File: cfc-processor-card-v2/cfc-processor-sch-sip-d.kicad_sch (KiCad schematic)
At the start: 4 parts, among them J3 Conn_01x02, U7 OSD3358-1G-ISM

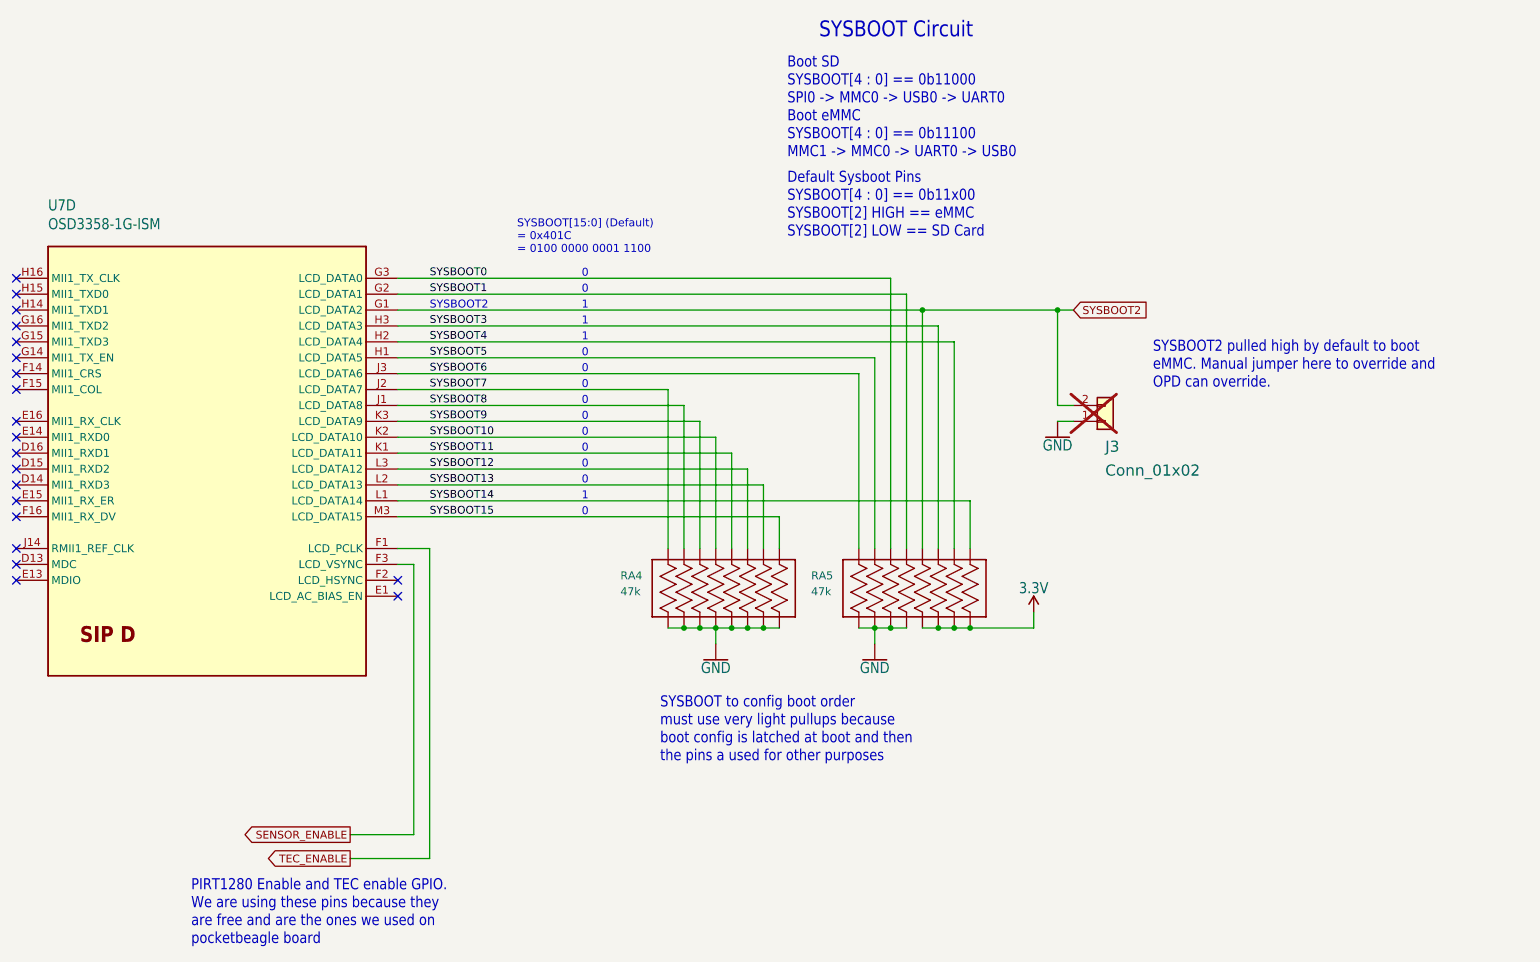
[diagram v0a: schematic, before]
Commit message: CFC processor schematic Change
changed to hierarchy view, changed all global net labels to hierarchy labels, changed all resistor, capacitor, and ground symbols to modern oresat labels. Deleted connectors sheet and added .history to gitignore.
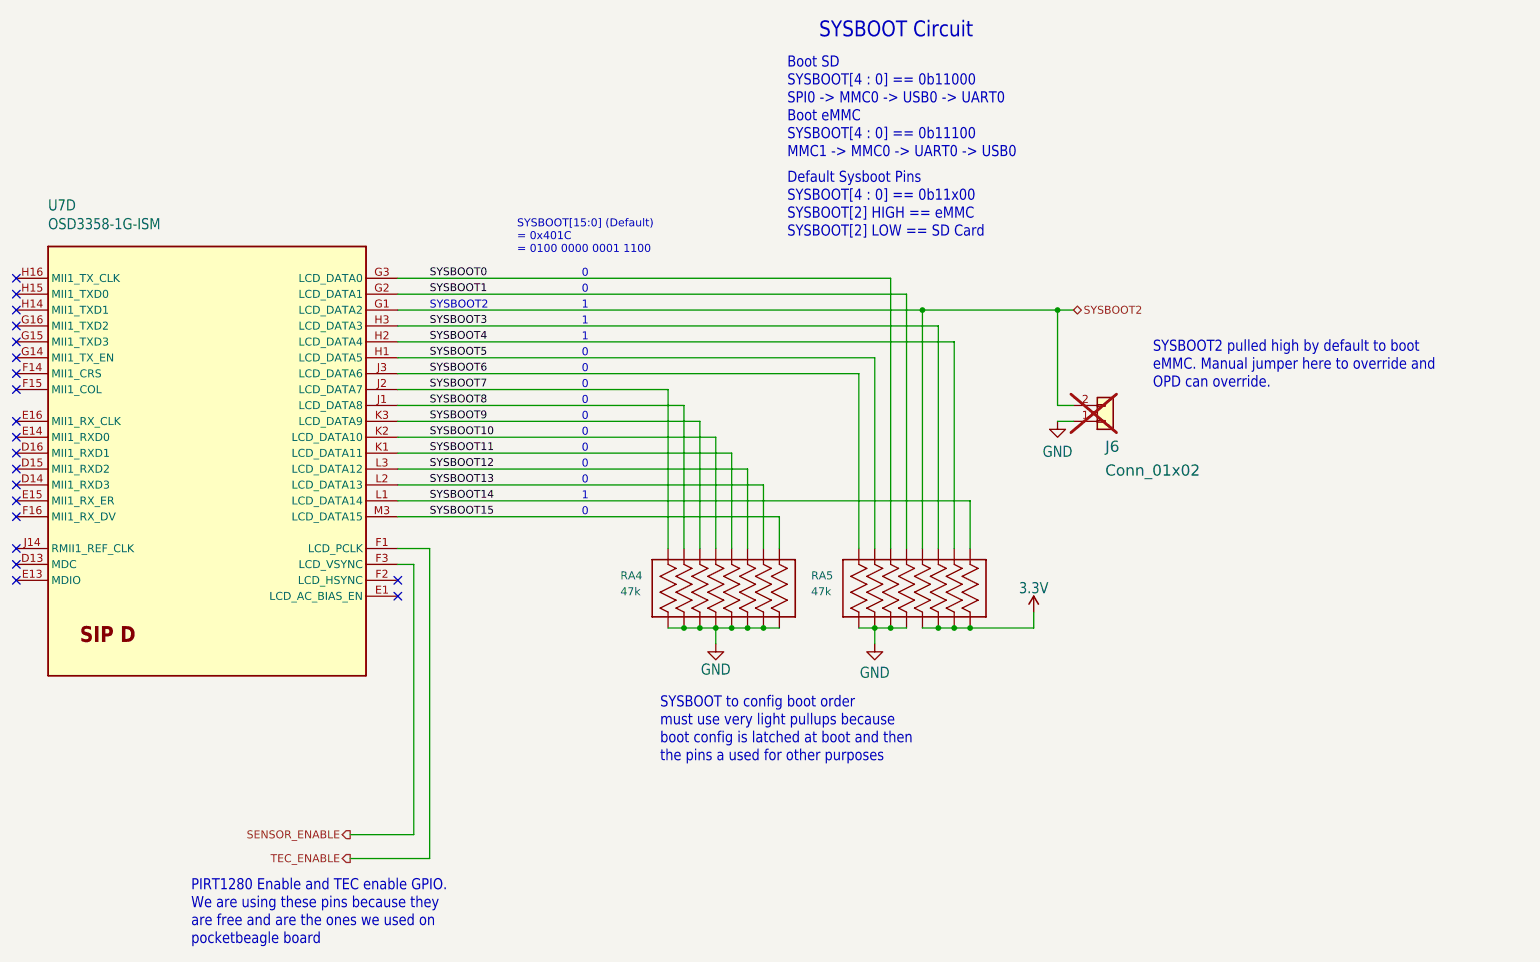
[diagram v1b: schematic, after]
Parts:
- renumbered J3 to J6

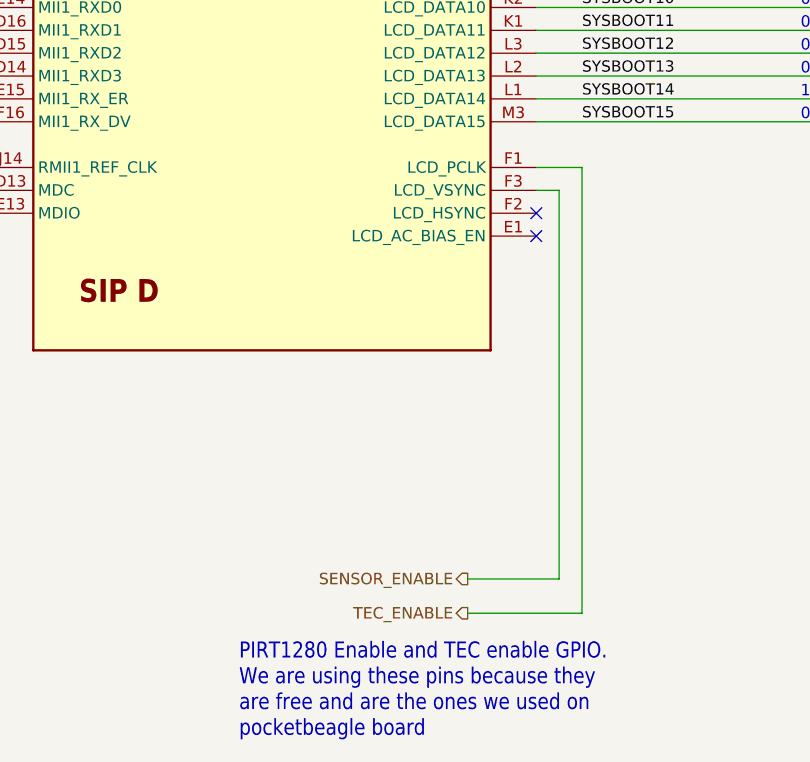
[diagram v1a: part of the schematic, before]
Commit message: Update
Added pull down resistors and removed therm + and sensor enable and added i2c support for cfc sensor card.
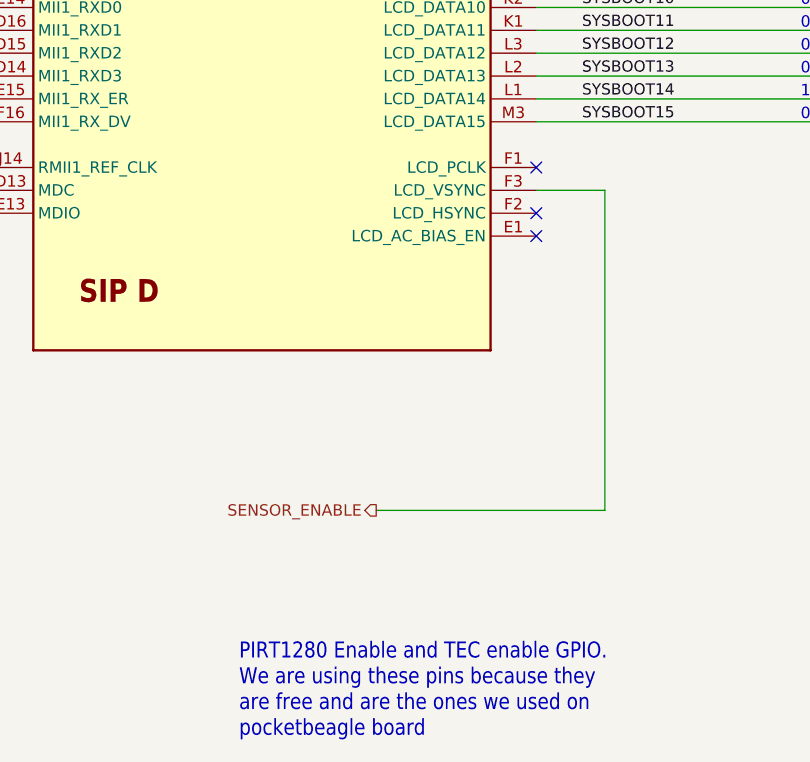
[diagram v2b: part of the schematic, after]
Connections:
- net TEC_ENABLE: no longer names the net of U7.F1 (LCD_PCLK)
- no-connect marks 20 -> 21
